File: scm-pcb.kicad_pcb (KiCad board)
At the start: 2 copper layers, 72.6 x 123.2 mm, 8 parts, among them J1 Raspberry_Pi_2_3, U2 MCP3008

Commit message: Updated PCB
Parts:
- J1: footprint Connector_PinHeader_2.54mm:PinHeader_2x20_P2.54mm_Vertical -> Rpi:MODULE_RASPBERRY_PI_3_MODEL_B+
- moved J1 50.7 mm to (128.7, 86.8)
- moved U2 49.6 mm to (123.0, 92.5), turned to 180 degrees
- moved REF** 49.5 mm to (173.8, 79.8), turned to 90 degrees
- moved C1 45.5 mm to (133.7, 114.3), turned to 180 degrees
- moved R1 35.6 mm to (129.6, 106.7), turned to 180 degrees
- moved R2 29.8 mm to (150.1, 100.4), turned to 90 degrees
- moved R3 28.2 mm to (136.7, 74.1), turned to -90 degrees
- moved D1 21.3 mm to (133.9, 106.7), turned to 0 degrees
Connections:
- C1 pad 3: (no net) -> Net-(D1-K)
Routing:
- net GND: track 129.0 -> 0.00 mm
- net Net-(#FLG03-pwr): track 124.1 -> 0.00 mm
- net Net-(D1-K): track 78.7 -> 0.00 mm
- net Net-(U2-CH2): track 35.1 -> 0.00 mm
- net +6V: track 31.4 -> 0.00 mm
- net Net-(J1-~{CE0}/GPIO8): track 26.3 -> 21.4 mm
- net Net-(J1-SCLK0/GPIO11): track 26.1 -> 21.2 mm
- net Net-(J1-MISO0/GPIO9): track 21.6 -> 17.4 mm
- net Net-(J1-MOSI0/GPIO10): track 29.2 -> 26.9 mm
- added copper zone on F.Cu, net +6V
- added copper zone on B.Cu, net GND
- added copper zone on F.Cu, net Net-(#FLG03-pwr)
- added copper zone on F.Cu, net Net-(D1-K)
- added copper zone on F.Cu, net Net-(U2-CH2)
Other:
- board size 72.6 x 123.2 mm -> 98 x 101.6 mm

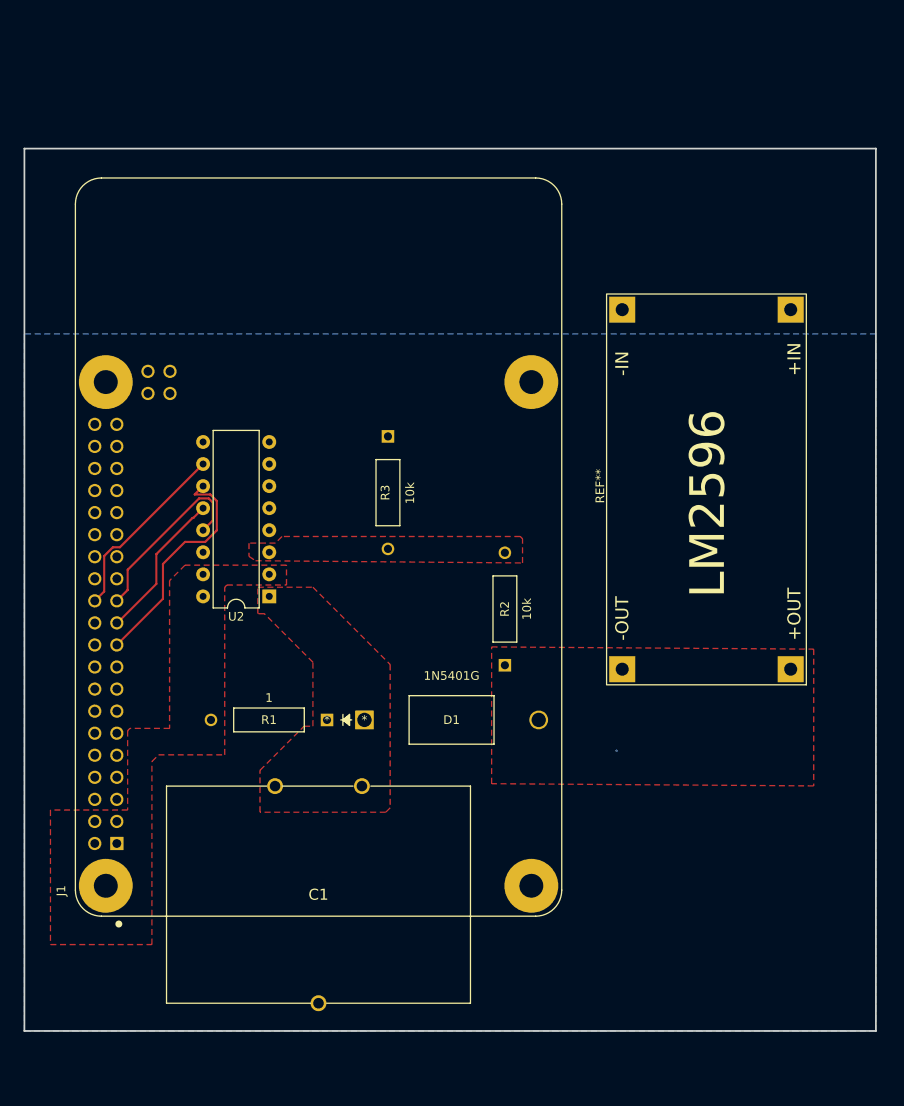
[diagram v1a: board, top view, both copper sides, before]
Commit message: Added ground via and cut corners (literally)
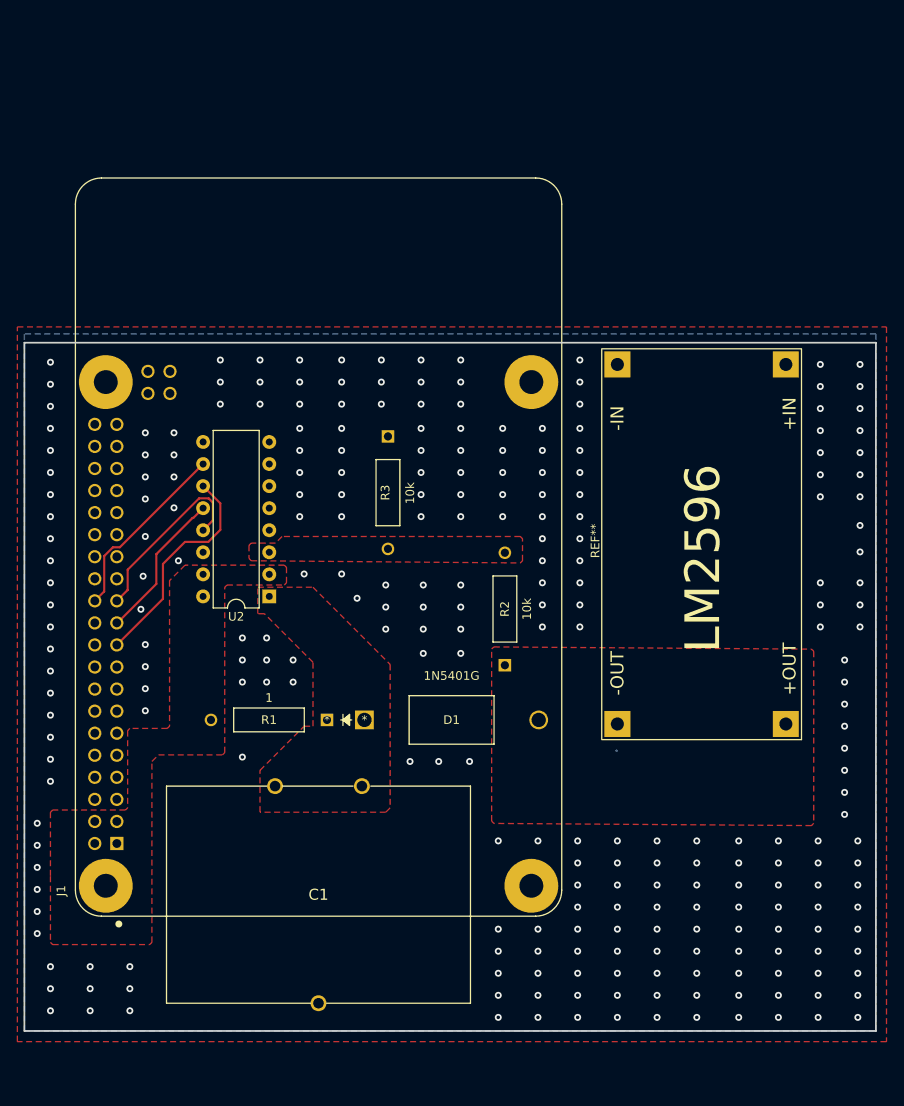
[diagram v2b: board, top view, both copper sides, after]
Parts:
- moved REF** 6.33 mm to (173.2, 86.1)
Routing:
- net Net-(J1-MOSI0/GPIO10): track 26.9 -> 25.6 mm
- net GND: vias 0 -> 260
- added copper zone on F.Cu, net GND
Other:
- board size 98 x 101.6 mm -> 98 x 79.2 mm

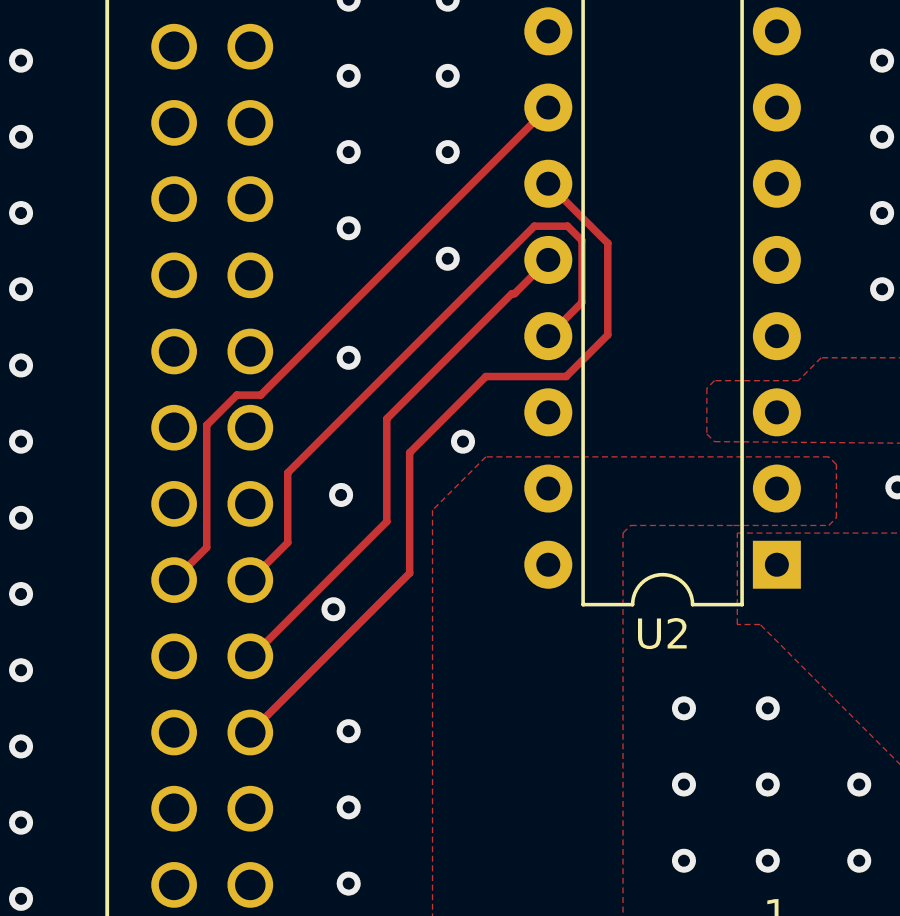
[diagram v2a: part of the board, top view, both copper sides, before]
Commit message: Added ground via and cut corners (literally)
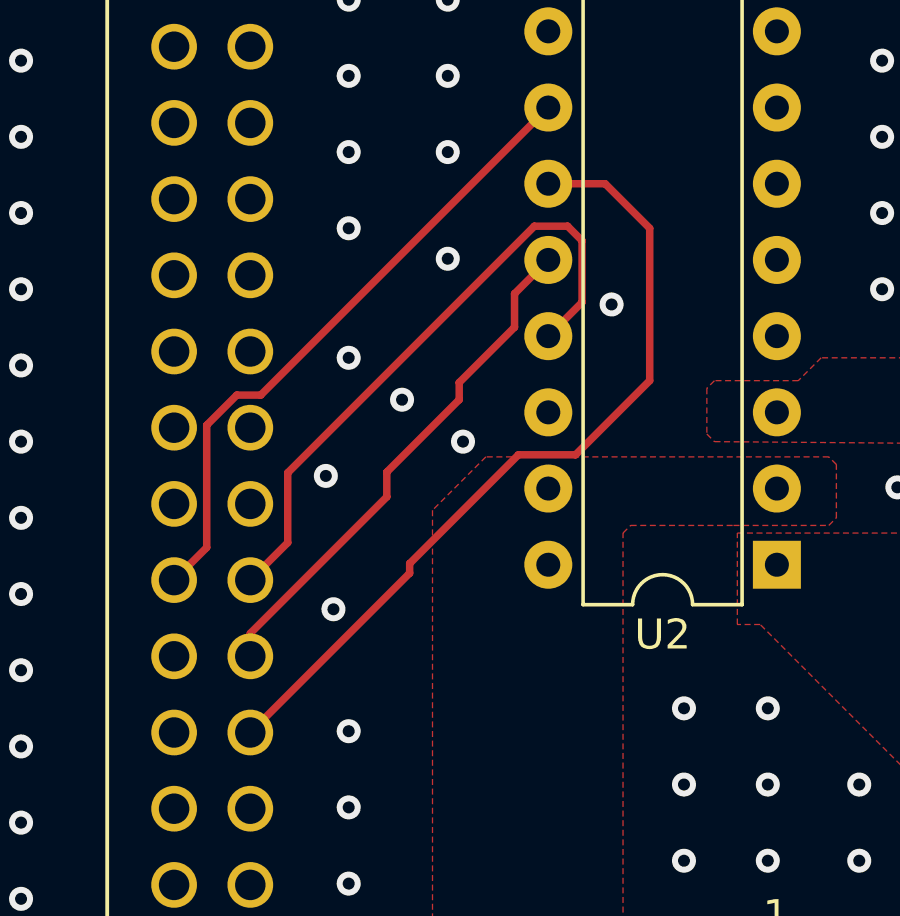
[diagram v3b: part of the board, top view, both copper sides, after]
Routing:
- net Net-(J1-MOSI0/GPIO10): track 25.6 -> 27.4 mm
- net GND: vias 260 -> 262
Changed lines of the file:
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@@
       (outputformat 1)
       (mirror false)
-      (drillshape 1)
+      (drillshape 0)
       (scaleselection 1)
-      (outputdirectory "")
+      (outputdirectory "../scm-pcb-gerber/")
     )
   )
@@
   (via (at 191.008 90.932) (size 0.8) (drill 0.4) (layers "F.Cu" "B.Cu") (free) (net 2))
   (via (at 186.436 78.486) (size 0.8) (drill 0.4) (layers "F.Cu" "B.Cu") (free) (net 2))
+  (via (at 107.95 89.535) (size 0.8) (drill 0.4) (layers "F.Cu" "B.Cu") (free) (net 2))
   (via (at 131.318 78.232) (size 0.8) (drill 0.4) (layers "F.Cu" "B.Cu") (free) (net 2))
   (via (at 172.212 133.35) (size 0.8) (drill 0.4) (layers "F.Cu" "B.Cu") (free) (net 2))
@@
   (via (at 186.436 75.946) (size 0.8) (drill 0.4) (layers "F.Cu" "B.Cu") (free) (net 2))
   (via (at 189.23 104.902) (size 0.8) (drill 0.4) (layers "F.Cu" "B.Cu") (free) (net 2))
+  (via (at 110.49 86.995) (size 0.8) (drill 0.4) (layers "F.Cu" "B.Cu") (free) (net 2))
   (via (at 189.23 117.602) (size 0.8) (drill 0.4) (layers "F.Cu" "B.Cu") (free) (net 2))
   (via (at 186.182 135.89) (size 0.8) (drill 0.4) (layers "F.Cu" "B.Cu") (free) (net 2))
@@
   (via (at 126.492 73.152) (size 0.8) (drill 0.4) (layers "F.Cu" "B.Cu") (free) (net 2))
   (via (at 97.79 85.852) (size 0.8) (drill 0.4) (layers "F.Cu" "B.Cu") (free) (net 2))
-  (via (at 108.458 90.17) (size 0.8) (drill 0.4) (layers "F.Cu" "B.Cu") (free) (net 2))
   (via (at 106.934 137.668) (size 0.8) (drill 0.4) (layers "F.Cu" "B.Cu") (free) (net 2))
   (via (at 186.436 70.866) (size 0.8) (drill 0.4) (layers "F.Cu" "B.Cu") (free) (net 2))
@@
   (via (at 163.068 133.35) (size 0.8) (drill 0.4) (layers "F.Cu" "B.Cu") (free) (net 2))
   (via (at 158.496 135.89) (size 0.8) (drill 0.4) (layers "F.Cu" "B.Cu") (free) (net 2))
+  (via (at 117.475 83.82) (size 0.8) (drill 0.4) (layers "F.Cu" "B.Cu") (free) (net 2))
   (via (at 158.75 78.232) (size 0.8) (drill 0.4) (layers "F.Cu" "B.Cu") (free) (net 2))
   (via (at 112.014 78.74) (size 0.8) (drill 0.4) (layers "F.Cu" "B.Cu") (free) (net 2))
@@
   (via (at 108.712 85.598) (size 0.8) (drill 0.4) (layers "F.Cu" "B.Cu") (free) (net 2))
   (via (at 97.79 96.012) (size 0.8) (drill 0.4) (layers "F.Cu" "B.Cu") (free) (net 2))
-  (segment (start 115.962 86.222) (end 113.284 86.222) (width 0.25) (layer "F.Cu") (net 20))
-  (segment (start 117.348 84.836) (end 115.962 86.222) (width 0.25) (layer "F.Cu") (net 20))
-  (segment (start 117.348 81.779) (end 117.348 84.836) (width 0.25) (layer "F.Cu") (net 20))
-  (segment (start 115.365 79.796) (end 117.348 81.779) (width 0.25) (layer "F.Cu") (net 20))
-  (segment (start 110.744 92.776) (end 105.432 98.088) (width 0.25) (layer "F.Cu") (net 20))
-  (segment (start 110.744 88.762) (end 110.744 92.776) (width 0.25) (layer "F.Cu") (net 20))
-  (segment (start 113.284 86.222) (end 110.744 88.762) (width 0.25) (layer "F.Cu") (net 20))
-  (segment (start 109.982 87.63) (end 109.982 91.059) (width 0.25) (layer "F.Cu") (net 22))
-  (segment (start 114.151 83.461) (end 109.982 87.63) (width 0.25) (layer "F.Cu") (net 22))
-  (segment (start 114.24 83.461) (end 114.151 83.461) (width 0.25) (layer "F.Cu") (net 22))
+  (segment (start 114.369 88.831) (end 116.274 88.831) (width 0.25) (layer "F.Cu") (net 20))
+  (segment (start 118.745 81.28) (end 117.261 79.796) (width 0.25) (layer "F.Cu") (net 20))
+  (segment (start 117.261 79.796) (end 115.365 79.796) (width 0.25) (layer "F.Cu") (net 20))
+  (segment (start 116.274 88.831) (end 118.745 86.36) (width 0.25) (layer "F.Cu") (net 20))
+  (segment (start 110.744 92.456) (end 114.369 88.831) (width 0.25) (layer "F.Cu") (net 20))
+  (segment (start 118.745 86.36) (end 118.745 81.28) (width 0.25) (layer "F.Cu") (net 20))
+  (segment (start 110.744 92.776) (end 110.744 92.456) (width 0.25) (layer "F.Cu") (net 20))
+  (segment (start 105.432 98.088) (end 110.744 92.776) (width 0.25) (layer "F.Cu") (net 20))
+  (segment (start 114.24 83.461) (end 114.24 84.5785) (width 0.25) (layer "F.Cu") (net 22))
+  (segment (start 112.395 86.995) (end 109.982 89.408) (width 0.25) (layer "F.Cu") (net 22))
+  (segment (start 109.982 90.2335) (end 105.432 94.7835) (width 0.25) (layer "F.Cu") (net 22))
+  (segment (start 109.982 89.408) (end 109.982 90.2335) (width 0.25) (layer "F.Cu") (net 22))
+  (segment (start 105.432 94.7835) (end 105.432 95.548) (width 0.25) (layer "F.Cu") (net 22))
   (segment (start 115.365 82.336) (end 114.24 83.461) (width 0.25) (layer "F.Cu") (net 22))
-  (segment (start 109.982 91.059) (end 105.493 95.548) (width 0.25) (layer "F.Cu") (net 22))
-  (segment (start 105.493 95.548) (end 105.432 95.548) (width 0.25) (layer "F.Cu") (net 22))
+  (segment (start 114.24 84.5785) (end 112.395 86.4235) (width 0.25) (layer "F.Cu") (net 22))
+  (segment (start 112.395 86.4235) (end 112.395 86.995) (width 0.25) (layer "F.Cu") (net 22))
   (segment (start 116.49 83.751) (end 116.49 81.692) (width 0.25) (layer "F.Cu") (net 24))
   (segment (start 106.68 89.430009) (end 106.68 91.76) (width 0.25) (layer "F.Cu") (net 24))
@@
   (zone (net 42) (net_name "Net-(U2-CH2)") (layer "F.Cu") (hatch edge 0.5)
     (priority 2)
-    (connect_pads (clearance 0.5))
+    (connect_pads yes (clearance 0.5))
     (min_thickness 0.25) (filled_areas_thickness no)
     (fill yes (thermal_gap 0.5) (thermal_bridge_width 0.5))

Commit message: updated PCB
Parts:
- C1: footprint Capacitors:MAL219690112E3 -> Capacitors:MAL219690102E3
- R1: value 1 -> .1; footprint Resistors:CPF11R0000FKEE6 -> Resistors:PAC100001007FA1000
- R2: value 10k -> 100k; footprint Resistors:CMF5510K000FKEB -> Resistors:MFR-25FRF52-100K
- moved R2 28.0 mm to (144.8, 72.9), turned to -90 degrees
- moved C1 13.6 mm to (128.9, 127.1)
- moved R3 5.55 mm to (131.3, 72.5)
- moved R1 0.72 mm to (130.4, 106.7)
- moved D1 0.71 mm to (134.7, 106.7)
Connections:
- C1 pad 1: Net-(D1-K) -> GND
- C1 pad 2: GND -> Net-(D1-K)
- R2 pad 1: +6V -> Solar_in
- REF** pad 3: (no net) -> GND
- REF** pad 4: (no net) -> Solar_in
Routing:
- net GND: vias 262 -> 193
- added copper zone on F.Cu, net Solar_in
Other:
- board size 98 x 79.2 mm -> 98 x 70.9 mm

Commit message: final commit
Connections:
- net Solar_in renamed +20V
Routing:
- net GND: vias 193 -> 186
